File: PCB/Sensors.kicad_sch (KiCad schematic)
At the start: 7 parts, among them U1 MS5611-01BA, U2 MMC5633NJL, U3 BMI088

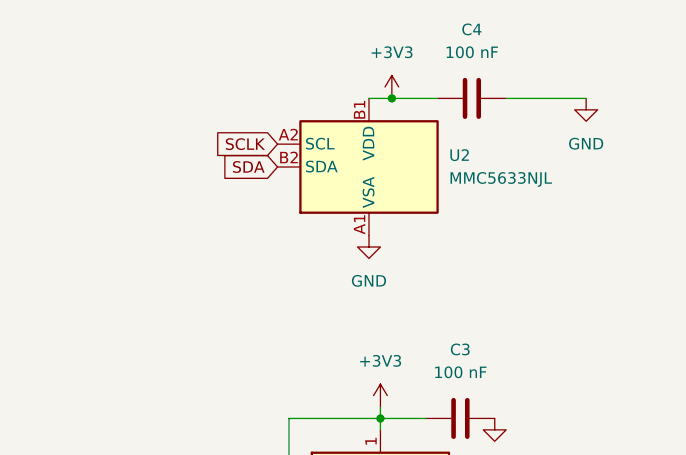
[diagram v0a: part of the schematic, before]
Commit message: removed MMC5603
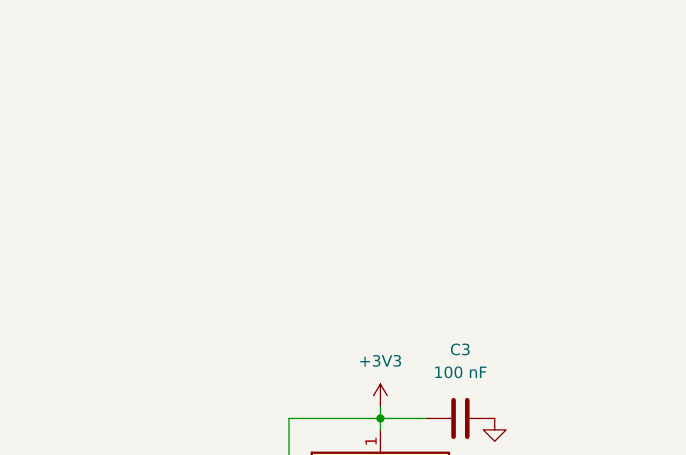
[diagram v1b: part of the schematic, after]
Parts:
- removed C4: 100 nF, Capacitor_SMD:C_0603_1608Metric, symbol Device:C
- removed U2: MMC5633NJL, Package_BGA:WLP-4_0.86x0.86mm_P0.4mm, symbol Sensor_Magnetic:MMC5633NJL
